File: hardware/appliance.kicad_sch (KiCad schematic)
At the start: 0 parts

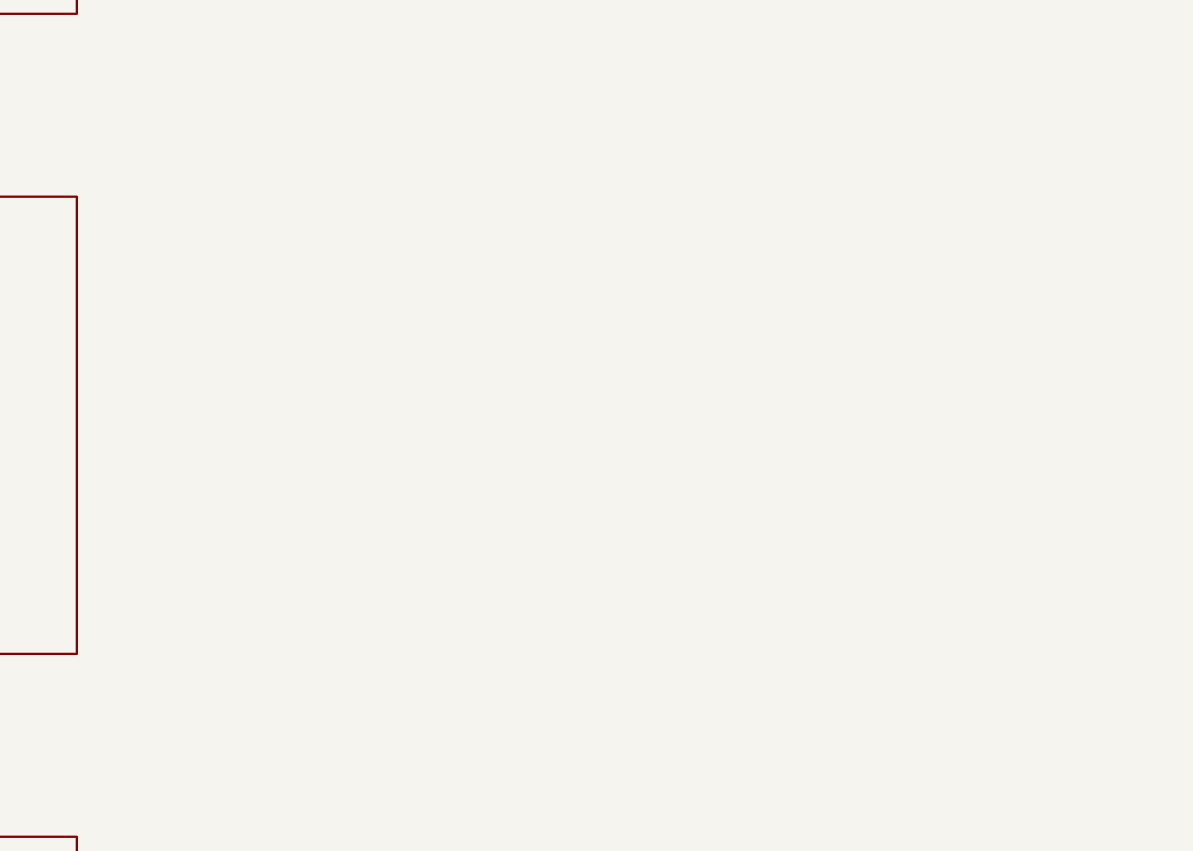
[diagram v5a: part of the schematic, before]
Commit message: Add processor logic and GPU local bypass banks
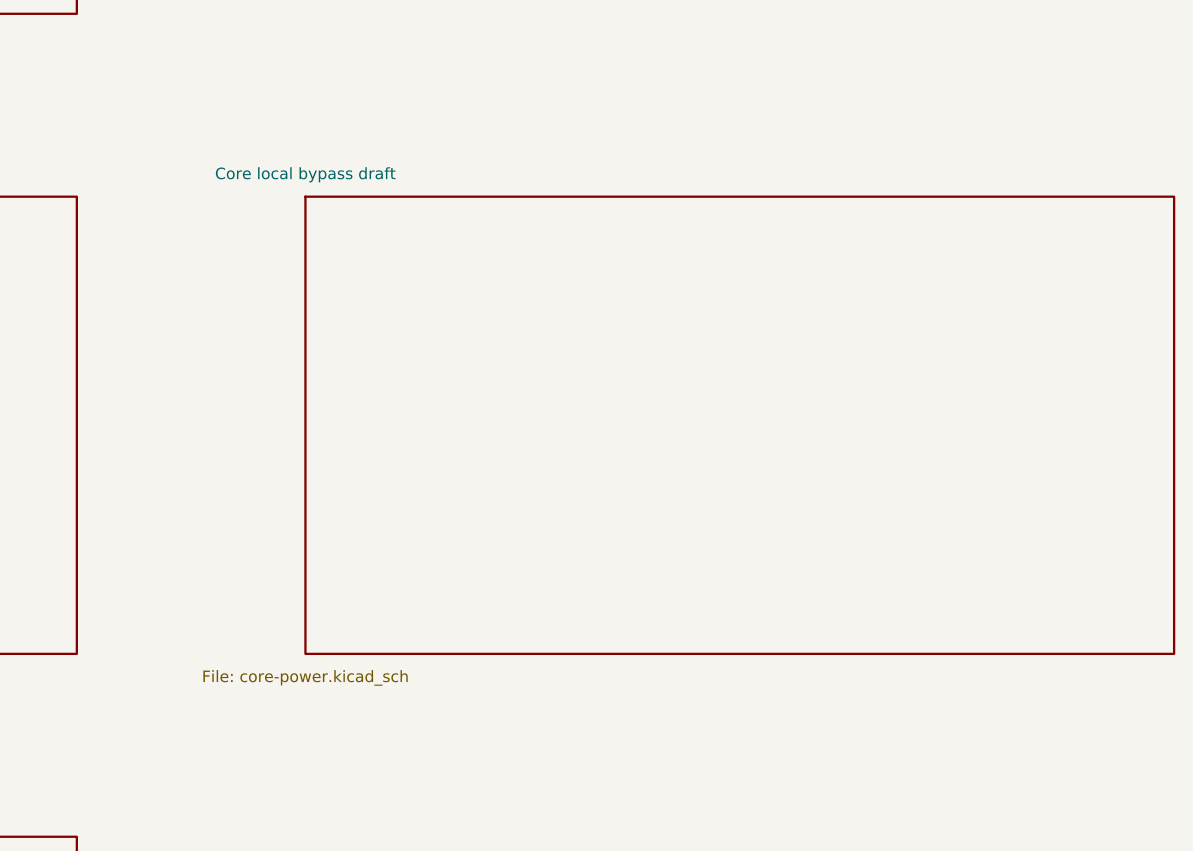
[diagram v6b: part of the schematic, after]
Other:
- added sheet Core local bypass draft (core-power.kicad_sch)

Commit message: Attach audited RAM draft and verify all ground connections
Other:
- added sheet Micron RAM draft (ram.kicad_sch)

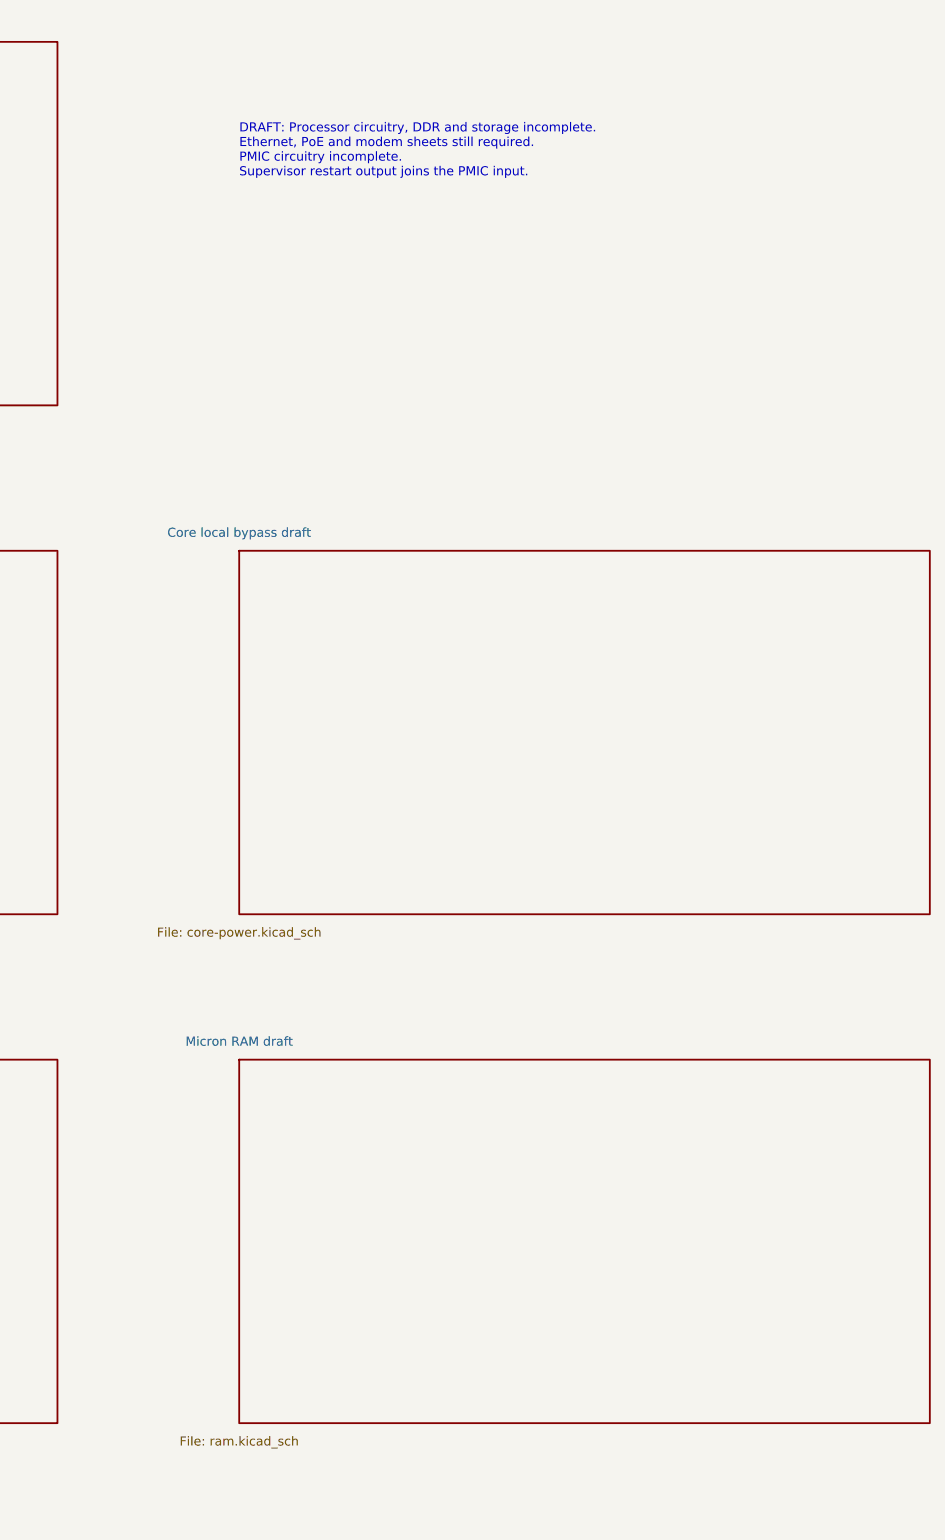
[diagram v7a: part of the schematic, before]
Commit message: Capture DDR BUCK3 supply and RAM VDD2 connections
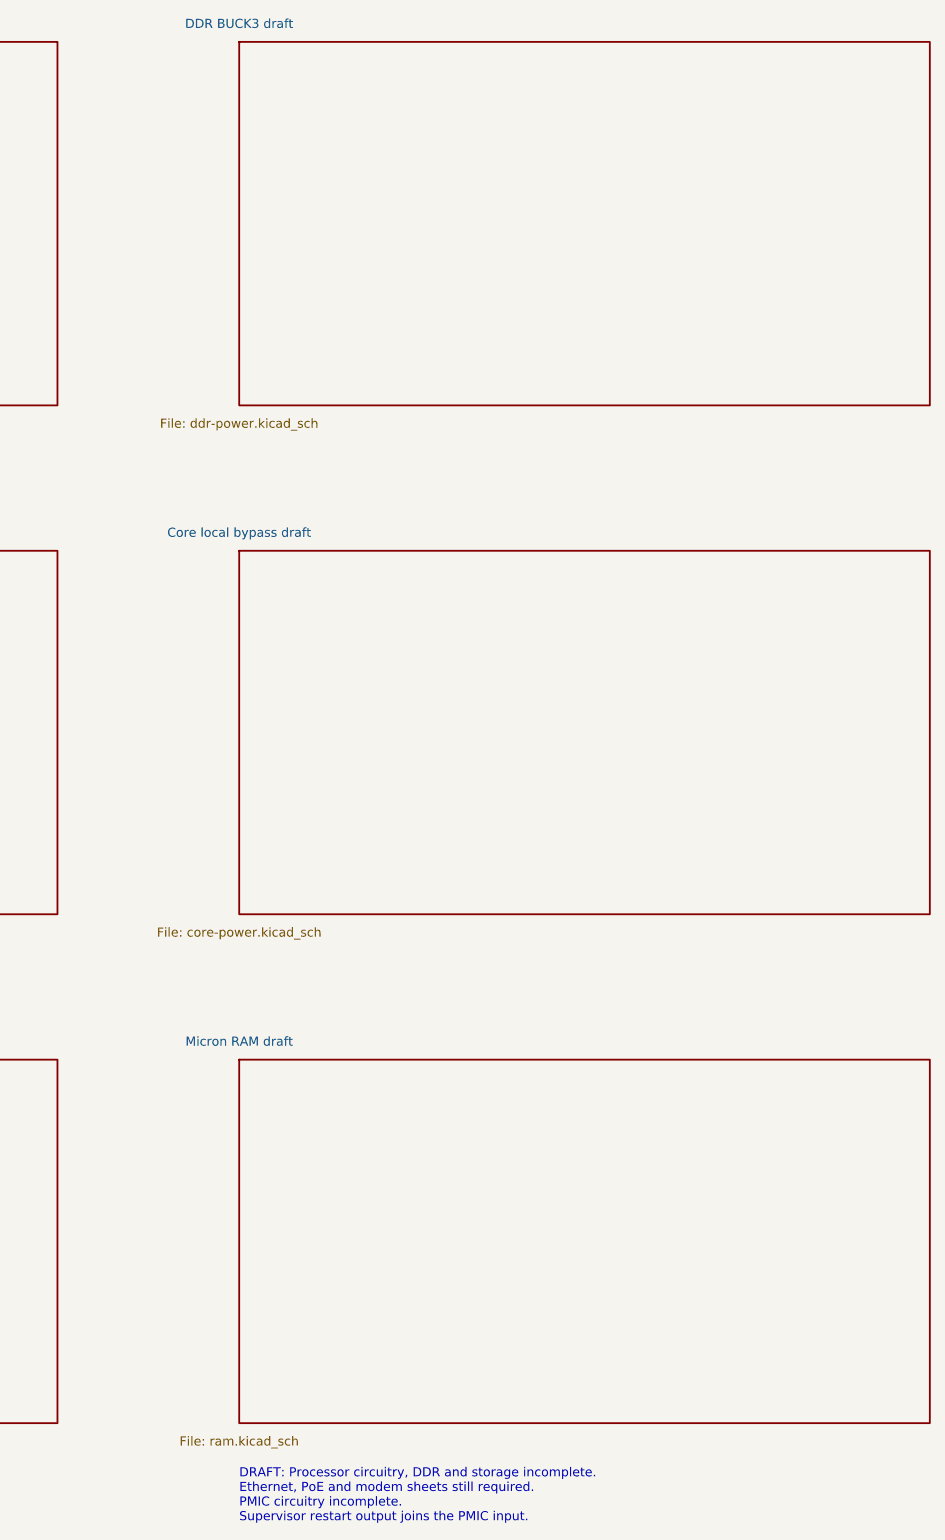
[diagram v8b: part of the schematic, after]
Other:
- added sheet DDR BUCK3 draft (ddr-power.kicad_sch)
